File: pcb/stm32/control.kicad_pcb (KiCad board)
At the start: 2 copper layers, 60 x 26 mm, 30 parts, among them J1 USB_C_Receptacle_USB2.0, J4 Term, P1 ST-Link, P2 ST-Link, P3 UG-2864ASWPG01, P4 har-flexicon 2,54 MSH-4, P5 WAGO2061-602, SW1 RotaryEncoder_Switch, U1 STM32G431CBUx, U2 TPS82130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

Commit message: Cleanup, add casing
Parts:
- removed R1: 10k, Resistor_SMD:R_0603_1608Metric
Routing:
- net SW: track 45.2 -> 21.8 mm, vias 2 -> 0
- net GND: track 203.7 -> 201.3 mm
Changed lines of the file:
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@@
-    )
-  )
-  (footprint "Resistor_SMD:R_0603_1608Metric" (layer "F.Cu")
-    (at 114.06 118.695 90)
-    (descr "Resistor SMD 0603 (1608 Metric), square (rectangular) end terminal, IPC_7351 nominal, (Body size source: IPC-SM-782 page 72, https://www.pcb-3d.com/wordpress/wp-content/uploads/ipc-sm-782a_amendment_1_and_2.pdf), generated with kicad-footprint-generator")
-    (tags "resistor")
-    (property "Sheetfile" "control.kicad_sch")
-    (property "Sheetname" "")
-    (property "ki_description" "Resistor")
-    (property "ki_keywords" "R res resistor")
-    (attr smd)
-    (fp_text reference "R1" (at -2.285 -0.01 90) (layer "F.SilkS")
-        (effects (font (size 1 1) (thickness 0.15)))
-    )
-    (fp_text value "10k" (at 0 1.43 90) (layer "F.Fab")
-        (effects (font (size 1 1) (thickness 0.15)))
-    )
-    (fp_text user "${REFERENCE}" (at 0 0 90) (layer "F.Fab")
-        (effects (font (size 0.4 0.4) (thickness 0.06)))
-    )
-    (fp_line (start -0.237258 -0.5225) (end 0.237258 -0.5225)
-      (stroke (width 0.12) (type solid)) (layer "F.SilkS"))
-    (fp_line (start -0.237258 0.5225) (end 0.237258 0.5225)
-      (stroke (width 0.12) (type solid)) (layer "F.SilkS"))
-    (fp_line (start -1.48 -0.73) (end 1.48 -0.73)
-      (stroke (width 0.05) (type solid)) (layer "F.CrtYd"))
-    (fp_line (start -1.48 0.73) (end -1.48 -0.73)
-      (stroke (width 0.05) (type solid)) (layer "F.CrtYd"))
-    (fp_line (start 1.48 -0.73) (end 1.48 0.73)
-      (stroke (width 0.05) (type solid)) (layer "F.CrtYd"))
-    (fp_line (start 1.48 0.73) (end -1.48 0.73)
-      (stroke (width 0.05) (type solid)) (layer "F.CrtYd"))
-    (fp_line (start -0.8 -0.4125) (end 0.8 -0.4125)
-      (stroke (width 0.1) (type solid)) (layer "F.Fab"))
-    (fp_line (start -0.8 0.4125) (end -0.8 -0.4125)
-      (stroke (width 0.1) (type solid)) (layer "F.Fab"))
-    (fp_line (start 0.8 -0.4125) (end 0.8 0.4125)
-      (stroke (width 0.1) (type solid)) (layer "F.Fab"))
-    (fp_line (start 0.8 0.4125) (end -0.8 0.4125)
-      (stroke (width 0.1) (type solid)) (layer "F.Fab"))
-    (pad "1" smd roundrect (at -0.825 0 90) (size 0.8 0.95) (layers "F.Cu" "F.Paste" "F.Mask") (roundrect_rratio 0.25)
-      (net 6 "SW") (pintype "passive"))
-    (pad "2" smd roundrect (at 0.825 0 90) (size 0.8 0.95) (layers "F.Cu" "F.Paste" "F.Mask") (roundrect_rratio 0.25)
-      (net 1 "GND") (pintype "passive"))
-    (model "${KICAD6_3DMODEL_DIR}/Resistor_SMD.3dshapes/R_0603_1608Metric.wrl"
-      (offset (xyz 0 0 0))
-      (scale (xyz 1 1 1))
-      (rotate (xyz 0 0 0))
     )
   )
@@
     (stroke (width 0.1) (type solid)) (fill none) (layer "Edge.Cuts"))
   (segment (start 92.25 125) (end 92.2 125.05) (width 0.5) (layer "F.Cu") (net 1))
-  (segment (start 112.6 116.15) (end 113.79 117.34) (width 0.2) (layer "F.Cu") (net 1))
   (segment (start 93 125) (end 92.25 125) (width 0.5) (layer "F.Cu") (net 1))
   (segment (start 101.75 112.45) (end 99.75 112.45) (width 0.5) (layer "F.Cu") (net 1))
@@
   (segment (start 82.085 124.225) (end 82.965 124.225) (width 0.5) (layer "F.Cu") (net 1))
   (segment (start 83.775 124.225) (end 83.8 124.2) (width 0.5) (layer "F.Cu") (net 1))
-  (segment (start 113.79 117.34) (end 113.79 117.6) (width 0.2) (layer "F.Cu") (net 1))
   (segment (start 103.83 131.26) (end 103.36 131.26) (width 0.5) (layer "F.Cu") (net 1))
   (segment (start 93 125) (end 93.65 125) (width 0.5) (layer "F.Cu") (net 1))
@@
   (segment (start 91.2 135.8) (end 91.2 136.9) (width 0.4) (layer "F.Cu") (net 1))
   (segment (start 103.83 131.26) (end 103.84 131.26) (width 0.5) (layer "F.Cu") (net 1))
-  (segment (start 113.79 117.6) (end 114.06 117.87) (width 0.2) (layer "F.Cu") (net 1))
   (segment (start 97.25 113.5) (end 97.25 112.45) (width 0.2) (layer "F.Cu") (net 1))
   (via (at 93 125) (size 0.6) (drill 0.3) (layers "F.Cu" "B.Cu") (net 1))
@@
   (segment (start 101.44 119.52) (end 114.06 119.52) (width 0.2) (layer "F.Cu") (net 6))
   (segment (start 100.725 121.125) (end 100.725 120.235) (width 0.2) (layer "F.Cu") (net 6))
-  (segment (start 99.225 127.9) (end 99.225 128.305) (width 0.2) (layer "F.Cu") (net 6))
-  (segment (start 99.225 128.305) (end 98.76 128.77) (width 0.2) (layer "F.Cu") (net 6))
   (segment (start 114.98 119.52) (end 119.5 115) (width 0.2) (layer "F.Cu") (net 6))
   (segment (start 114.06 119.52) (end 114.98 119.52) (width 0.2) (layer "F.Cu") (net 6))
   (segment (start 100.725 120.235) (end 100.86 120.1) (width 0.2) (layer "F.Cu") (net 6))
-  (via (at 100.86 120.1) (size 0.6) (drill 0.3) (layers "F.Cu" "B.Cu") (net 6))
-  (via (at 98.76 128.77) (size 0.6) (drill 0.3) (layers "F.Cu" "B.Cu") (net 6))
-  (segment (start 95.88 119.92) (end 100.68 119.92) (width 0.2) (layer "B.Cu") (net 6))
-  (segment (start 94.13 122.24) (end 94.13 121.67) (width 0.2) (layer "B.Cu") (net 6))
-  (segment (start 94.13 121.67) (end 95.88 119.92) (width 0.2) (layer "B.Cu") (net 6))
-  (segment (start 97.68 123.52) (end 97.68 122.85) (width 0.2) (layer "B.Cu") (net 6))
-  (segment (start 100.68 119.92) (end 100.86 120.1) (width 0.2) (layer "B.Cu") (net 6))
-  (segment (start 97.4 122.57) (end 94.46 122.57) (width 0.2) (layer "B.Cu") (net 6))
-  (segment (start 98.76 128.77) (end 97.26 127.27) (width 0.2) (layer "B.Cu") (net 6))
-  (segment (start 94.59 125.95) (end 96.4 124.14) (width 0.2) (layer "B.Cu") (net 6))
-  (segment (start 97.26 127.27) (end 95.34 127.27) (width 0.2) (layer "B.Cu") (net 6))
-  (segment (start 94.46 122.57) (end 94.13 122.24) (width 0.2) (layer "B.Cu") (net 6))
-  (segment (start 97.68 122.85) (end 97.4 122.57) (width 0.2) (layer "B.Cu") (net 6))
-  (segment (start 95.34 127.27) (end 94.59 126.52) (width 0.2) (layer "B.Cu") (net 6))
-  (segment (start 94.59 126.52) (end 94.59 125.95) (width 0.2) (layer "B.Cu") (net 6))
-  (segment (start 96.4 124.14) (end 97.06 124.14) (width 0.2) (layer "B.Cu") (net 6))
-  (segment (start 97.06 124.14) (end 97.68 123.52) (width 0.2) (layer "B.Cu") (net 6))
   (segment (start 103.24 123.75) (end 102.85 123.75) (width 0.2) (layer "F.Cu") (net 7))
   (segment (start 99.53 128.89) (end 98.69 129.73) (width 0.2) (layer "F.Cu") (net 7))

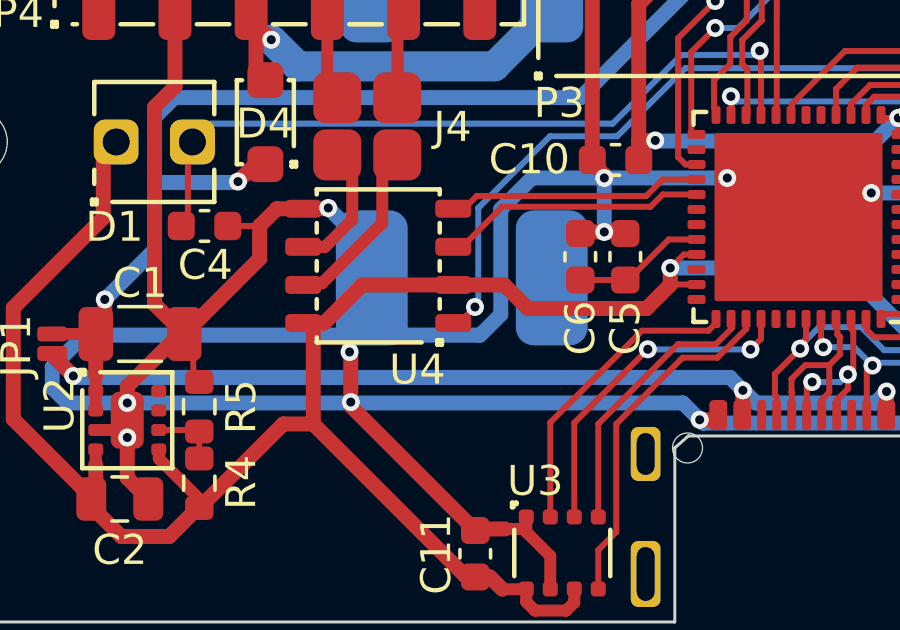
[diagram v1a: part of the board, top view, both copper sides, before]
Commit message: Control brightness and duraton with remote control
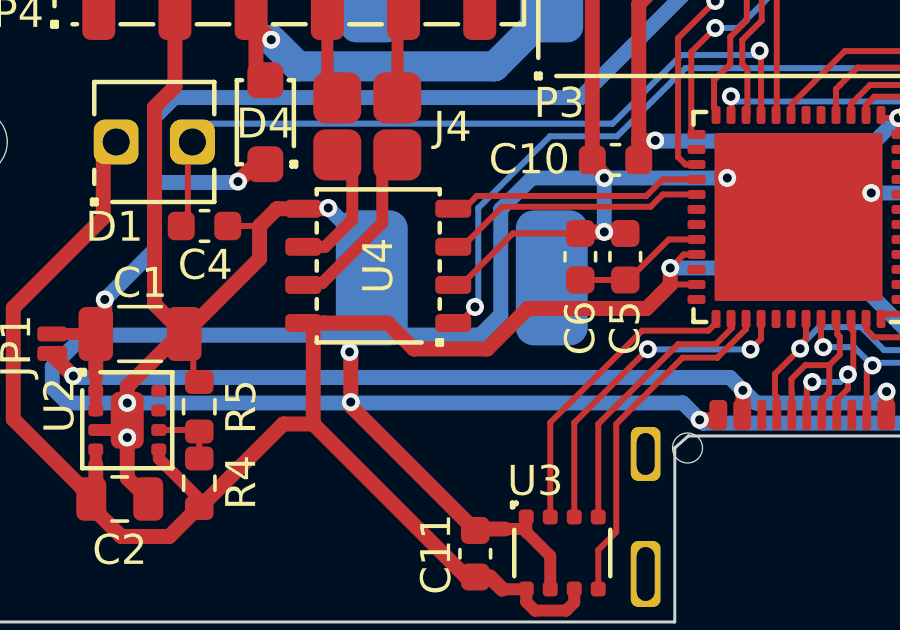
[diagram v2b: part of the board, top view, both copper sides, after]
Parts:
- U4: footprint local:SP3485 -> local:SO-8
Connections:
- U1 pad 30: SW -> unconnected-(U1-PA8-Pad30)
- U4 pad 2: +3V3 -> GND
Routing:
- net GND: track 201.3 -> 206.3 mm
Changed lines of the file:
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@@
   (net 64 "unconnected-(U2-PG-Pad7)")
   (net 65 "unconnected-(U2-SS{slash}TR-Pad8)")
+  (net 66 "unconnected-(U1-PA8-Pad30)")
   (footprint "Capacitor_SMD:C_0603_1608Metric" (layer "F.Cu")
     (at 88.7 135.725 90)
@@
     )
   )
-  (footprint "local:SP3485" (layer "F.Cu")
+  (footprint "local:SO-8" (layer "F.Cu")
     (at 85.465 126.13 90)
-    (descr "RS-485 Transceiver 3.3V")
+    (descr "Generic SO-8 footprint (https://en.wikipedia.org/wiki/Small_outline_integrated_circuit)")
     (property "Sheetfile" "control.kicad_sch")
     (property "Sheetname" "")
@@
     (property "ki_keywords" "Low Power Half-Duplex RS-485 Transceiver 10Mbps")
     (attr smd)
-    (fp_text reference "U4" (at -3.46 1.305 180) (layer "F.SilkS")
-        (effects (font (size 1 1) (thickness 0.15)))
-    )
-    (fp_text value "SP3485CN" (at -0.01 -1.655 90) (layer "F.Fab")
+    (fp_text reference "U4" (at 0 0 90) (layer "F.SilkS")
+        (effects (font (size 1 1) (thickness 0.15)))
+    )
+    (fp_text value "SP3485CN" (at 0 0 90) (layer "F.Fab")
         (effects (font (size 1 1) (thickness 0.15)))
     )
@@
       (net 28 "RS485_RX") (pinfunction "RO") (pintype "output"))
     (pad "2" smd roundrect (at -0.635 2.5 90) (size 0.6 1.2) (layers "F.Cu" "F.Paste" "F.Mask") (roundrect_rratio 0.25)
-      (net 2 "+3V3") (pinfunction "~{RE}") (pintype "input"))
+      (net 1 "GND") (pinfunction "~{RE}") (pintype "input"))
     (pad "3" smd roundrect (at 0.635 2.5 90) (size 0.6 1.2) (layers "F.Cu" "F.Paste" "F.Mask") (roundrect_rratio 0.25)
       (net 15 "RS485_DE") (pinfunction "DE") (pintype "input"))
@@
     (pad "8" smd roundrect (at -1.905 -2.5 90) (size 0.6 1.2) (layers "F.Cu" "F.Paste" "F.Mask") (roundrect_rratio 0.25)
       (net 2 "+3V3") (pinfunction "VCC") (pintype "power_in"))
-    (model "SP3485.wrl"
+    (model "SO-8.wrl"
       (offset (xyz 0 0 0))
       (scale (xyz 1 1 1))
@@
       (net 19 "unconnected-(U1-PC6-Pad29)") (pinfunction "PC6") (pintype "bidirectional"))
     (pad "30" smd roundrect (at 0.25 -3.4 180) (size 0.3 0.6) (layers "F.Cu" "F.Paste" "F.Mask") (roundrect_rratio 0.25)
-      (net 6 "SW") (pinfunction "PA8") (pintype "bidirectional"))
+      (net 66 "unconnected-(U1-PA8-Pad30)") (pinfunction "PA8") (pintype "bidirectional"))
     (pad "31" smd roundrect (at -0.25 -3.4 180) (size 0.3 0.6) (layers "F.Cu" "F.Paste" "F.Mask") (roundrect_rratio 0.25)
       (net 7 "USB_CC1") (pinfunction "PA9") (pintype "bidirectional"))
@@
   (segment (start 103.84 131.26) (end 104.2 130.9) (width 0.5) (layer "F.Cu") (net 1))
   (segment (start 101.75 113.5) (end 101.75 112.45) (width 0.2) (layer "F.Cu") (net 1))
+  (segment (start 89.95 125.05) (end 92.2 125.05) (width 0.2) (layer "F.Cu") (net 1))
   (segment (start 116.1 136.4) (end 116.1 135.4) (width 0.2) (layer "F.Cu") (net 1))
+  (segment (start 87.965 126.765) (end 88.235 126.765) (width 0.2) (layer "F.Cu") (net 1))
   (segment (start 95.25 113.5) (end 95.25 112.45) (width 0.2) (layer "F.Cu") (net 1))
   (segment (start 78.69 120.16) (end 78.01 120.84) (width 0.5) (layer "F.Cu") (net 1))
@@
   (segment (start 93.65 125) (end 93.7 125.05) (width 0.5) (layer "F.Cu") (net 1))
   (segment (start 103.75 112.45) (end 103.25 112.45) (width 0.5) (layer "F.Cu") (net 1))
+  (segment (start 88.235 126.765) (end 89.95 125.05) (width 0.2) (layer "F.Cu") (net 1))
   (segment (start 103.25 113.5) (end 103.25 112.45) (width 0.2) (layer "F.Cu") (net 1))
   (segment (start 94.75 112.45) (end 94.25 112.45) (width 0.5) (layer "F.Cu") (net 1))
@@
   (segment (start 75.9 133.9) (end 75.9 134.15) (width 0.4) (layer "F.Cu") (net 2))
   (segment (start 73.3 127.53) (end 76.3 124.53) (width 0.5) (layer "F.Cu") (net 2))
-  (segment (start 89.665 126.765) (end 87.965 126.765) (width 0.5) (layer "F.Cu") (net 2))
   (segment (start 78.15 132.55) (end 79.5 133.9) (width 0.4) (layer "F.Cu") (net 2))
   (segment (start 76.3 122.43) (end 76.73 122) (width 0.5) (layer "F.Cu") (net 2))
@@
   (segment (start 110.9 135.15) (end 111.25 134.8) (width 0.4) (layer "F.Cu") (net 2))
   (segment (start 76.9 135.15) (end 78.5 135.15) (width 0.5) (layer "F.Cu") (net 2))
+  (segment (start 83.665 128.035) (end 85.785 128.035) (width 0.5) (layer "F.Cu") (net 2))
   (segment (start 96.25 114.6) (end 96.25 115.3) (width 0.5) (layer "F.Cu") (net 2))
   (segment (start 95.21 126.75) (end 96.1 126.75) (width 0.2) (layer "F.Cu") (net 2))
@@
   (segment (start 103.16 128.37) (end 103.02 128.51) (width 0.2) (layer "F.Cu") (net 2))
   (segment (start 75.9 134.15) (end 76.9 135.15) (width 0.5) (layer "F.Cu") (net 2))
+  (segment (start 89.1 128.9) (end 90.45 127.55) (width 0.5) (layer "F.Cu") (net 2))
   (segment (start 94.15 121.95) (end 94.15 122.7) (width 0.5) (layer "F.Cu") (net 2))
+  (segment (start 85.785 128.035) (end 86.65 128.9) (width 0.5) (layer "F.Cu") (net 2))
   (segment (start 94.88 127.08) (end 95.21 126.75) (width 0.2) (layer "F.Cu") (net 2))
-  (segment (start 84.935 126.765) (end 87.965 126.765) (width 0.5) (layer "F.Cu") (net 2))
   (segment (start 82.3 131.4) (end 83.3 131.4) (width 0.5) (layer "F.Cu") (net 2))
   (segment (start 83.3 131.4) (end 88.4 136.5) (width 0.5) (layer "F.Cu") (net 2))
@@
   (segment (start 88.4 136.5) (end 89.19 136.5) (width 0.5) (layer "F.Cu") (net 2))
   (segment (start 76.3 124.53) (end 76.3 122.43) (width 0.5) (layer "F.Cu") (net 2))
-  (segment (start 90.45 127.55) (end 89.665 126.765) (width 0.5) (layer "F.Cu") (net 2))
   (segment (start 78.5 135.15) (end 79.45 134.2) (width 0.5) (layer "F.Cu") (net 2))
   (segment (start 96.25 113.5) (end 96.25 114.6) (width 0.2) (layer "F.Cu") (net 2))
@@
   (segment (start 101.75 128.26) (end 101.75 128.01) (width 0.2) (layer "F.Cu") (net 2))
   (segment (start 76.05 133.75) (end 75.9 133.9) (width 0.5) (layer "F.Cu") (net 2))
+  (segment (start 86.65 128.9) (end 89.1 128.9) (width 0.5) (layer "F.Cu") (net 2))
   (segment (start 92 136.9) (end 92 137.35) (width 0.4) (layer "F.Cu") (net 2))
   (segment (start 94.88 127.08) (end 95.2 126.76) (width 0.5) (layer "F.Cu") (net 2))
-  (segment (start 83.665 128.035) (end 84.935 126.765) (width 0.5) (layer "F.Cu") (net 2))
   (segment (start 95.65 125.75) (end 96.1 125.75) (width 0.2) (layer "F.Cu") (net 2))
   (segment (start 83.3 128.37) (end 83.3 131.4) (width 0.5) (layer "F.Cu") (net 2))

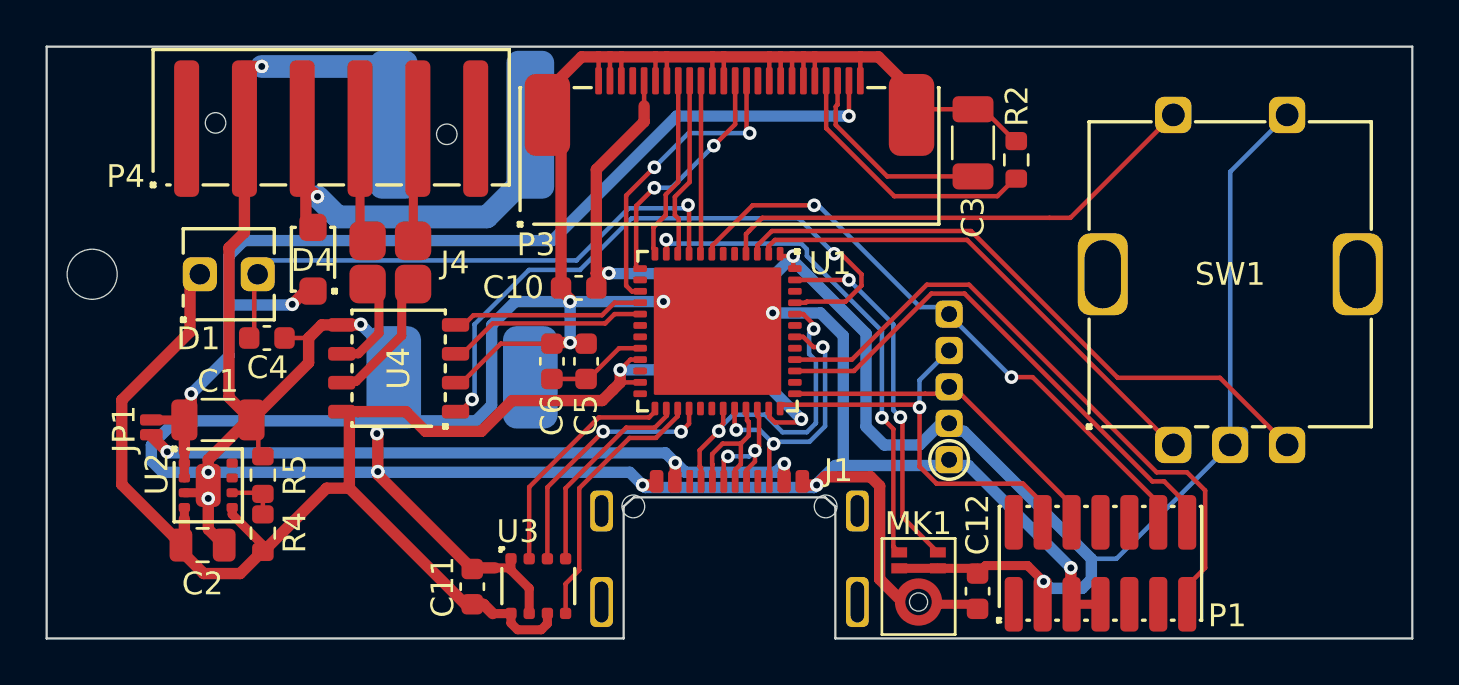
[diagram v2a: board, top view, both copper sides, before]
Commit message: Add SnowSparkle, new footprints
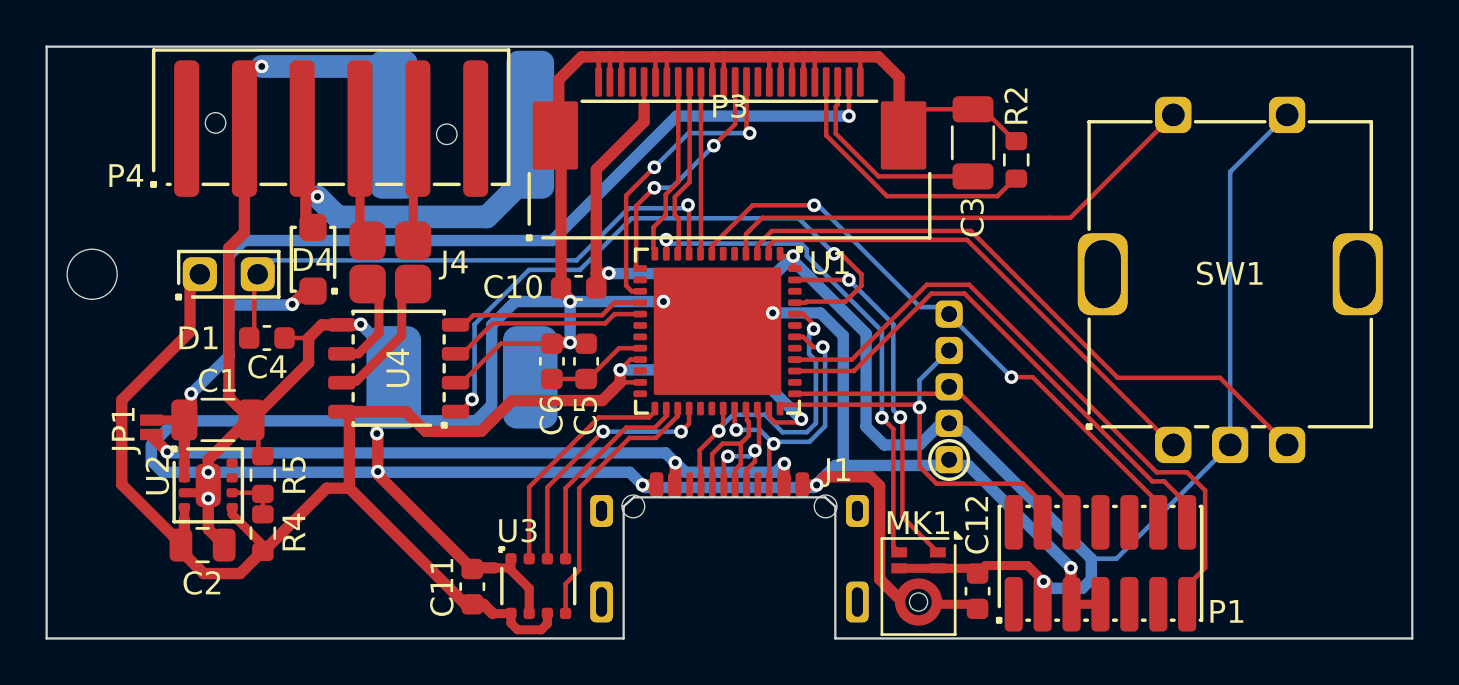
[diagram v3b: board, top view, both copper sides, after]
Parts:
- P1: value ST-Link -> FTSH-107-01-L-DV-K; footprint local:FTSH-107-01-L-DV-K -> local:PinHeader-2x7-1.27mm-smd
- P3: footprint local:Connector-Flat-24_P0.5mm -> local:Connector-Flat-24-0.5mm
- moved P3 0.35 mm to (100.0, 114.7)
- turned U2 to 0 degrees
